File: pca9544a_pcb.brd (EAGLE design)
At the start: 43 x 43 mm, 37 parts, among them IC1 PCA9544ABS, X6 TSW-102-02-S-S-RA, X7 TSW-102-02-S-S-RA, X8 TSW-102-02-S-S-RA, X9 TSW-102-02-S-S-RA

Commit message: gerber out
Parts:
- GIT1: value b5c31e5 -> dcc5f2d
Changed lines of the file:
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@@
 </autorouter>
 <elements>
-<element name="GIT1" library="git-revision" package="GIT-REVISION_1.2" value="b5c31e5" x="32" y="37">
+<element name="GIT1" library="git-revision" package="GIT-REVISION_1.2" value="dcc5f2d" x="32" y="37">
 <attribute name="NOT_COMPONENT" value="YES" x="32" y="37" size="1.778" layer="27" display="off"/>
 </element>

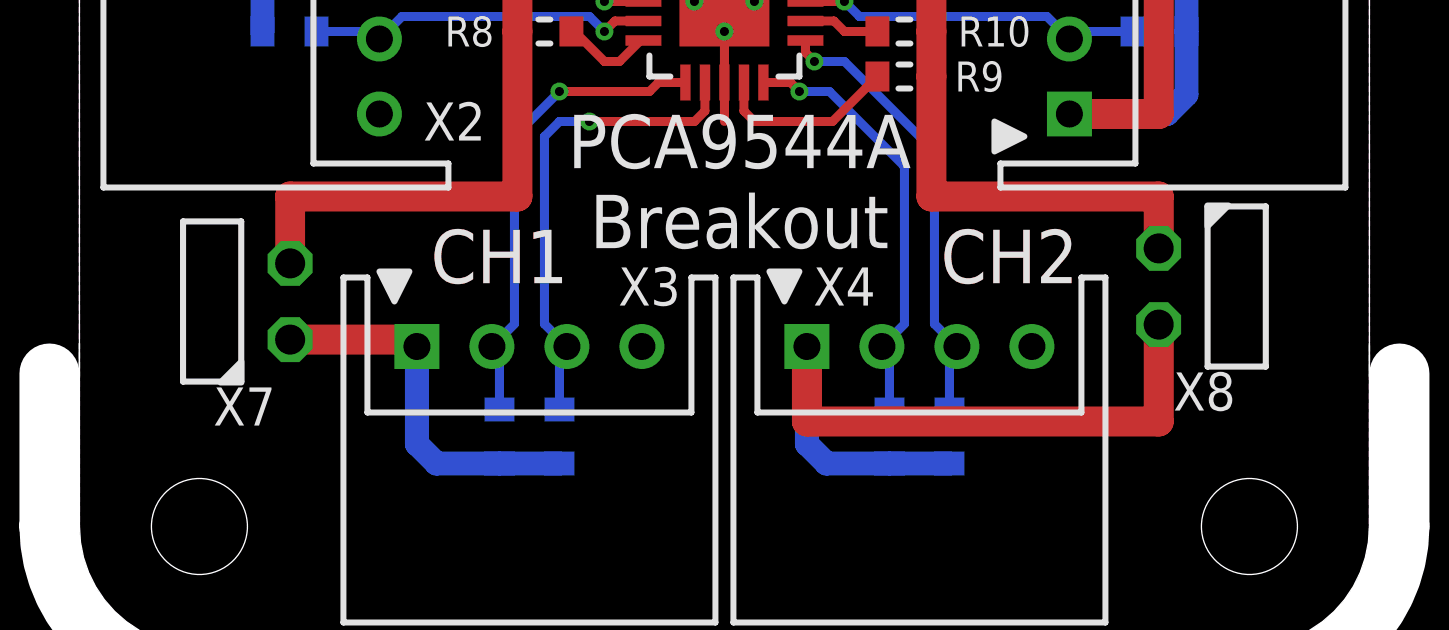
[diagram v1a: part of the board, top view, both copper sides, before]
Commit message: moved X7 and X8 headers
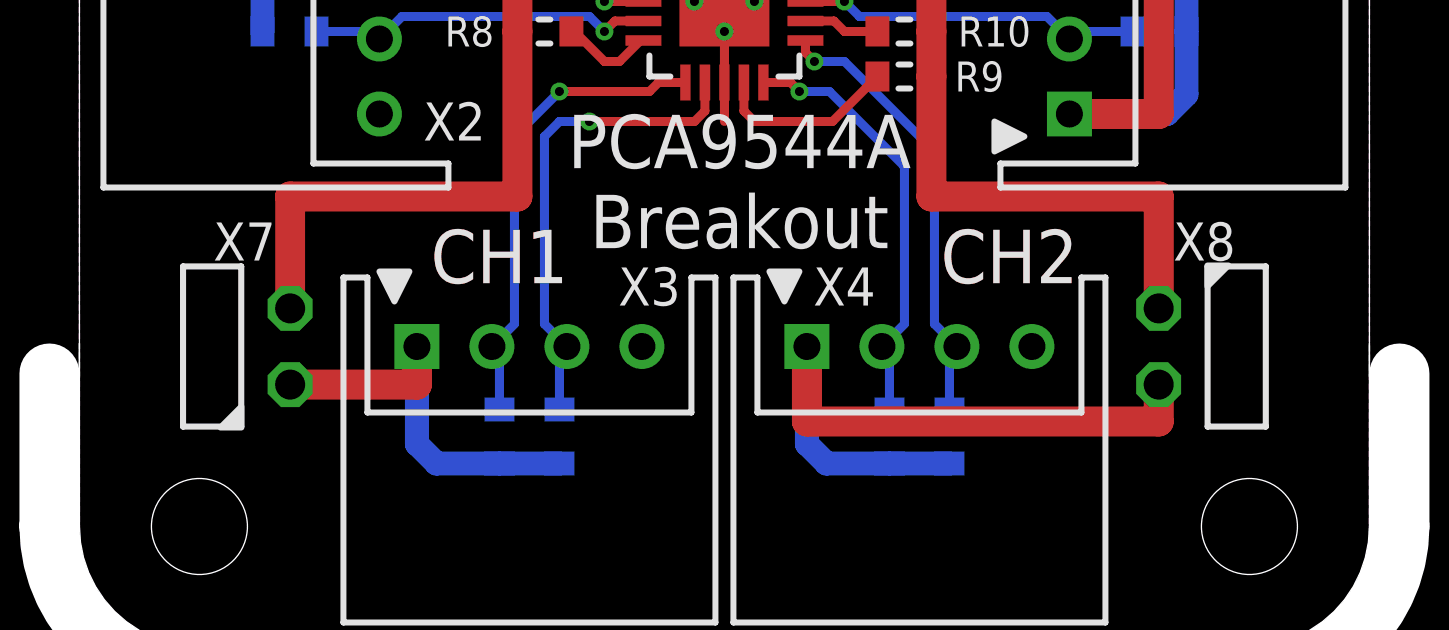
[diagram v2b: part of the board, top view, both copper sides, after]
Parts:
- moved X8 2.00 mm to (37.5, 10.0)
- moved X7 1.50 mm to (5.50, 10.0)
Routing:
- net VCC: track 96.7 -> 100.2 mm
- net N$21: track 25.7 -> 23.7 mm
- net N$20: track 12.7 -> 13.8 mm
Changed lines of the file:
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@@
 <attribute name="VALUE" x="-1.5" y="26.6" size="1" layer="27" ratio="20"/>
 </element>
-<element name="X7" library="con-samtec.local" package="TSW-102-02-S-S-RA" value="TSW-102-02-S-S-RA" x="5.5" y="11.5" smashed="yes" rot="R270">
-<attribute name="NAME" x="5.5" y="8" size="1.27" layer="25" ratio="16" align="center"/>
-<attribute name="VALUE" x="-1.5" y="7.1" size="1" layer="27" ratio="20"/>
+<element name="X7" library="con-samtec.local" package="TSW-102-02-S-S-RA" value="TSW-102-02-S-S-RA" x="5.5" y="10" smashed="yes" rot="R270">
+<attribute name="NAME" x="5.5" y="13.5" size="1.27" layer="25" ratio="16" align="center"/>
+<attribute name="VALUE" x="-1.5" y="5.6" size="1" layer="27" ratio="20"/>
 </element>
-<element name="X8" library="con-samtec.local" package="TSW-102-02-S-S-RA" value="TSW-102-02-S-S-RA" x="37.5" y="12" smashed="yes" rot="R90">
-<attribute name="NAME" x="37.5" y="8.5" size="1.27" layer="25" ratio="16" rot="R180" align="center"/>
-<attribute name="VALUE" x="44.5" y="16.4" size="1" layer="27" ratio="20" rot="R180"/>
+<element name="X8" library="con-samtec.local" package="TSW-102-02-S-S-RA" value="TSW-102-02-S-S-RA" x="37.5" y="10" smashed="yes" rot="R90">
+<attribute name="NAME" x="37.5" y="13.5" size="1.27" layer="25" ratio="16" rot="R180" align="center"/>
+<attribute name="VALUE" x="44.5" y="14.4" size="1" layer="27" ratio="20" rot="R180"/>
 </element>
 <element name="X9" library="con-samtec.local" package="TSW-102-02-S-S-RA" value="TSW-102-02-S-S-RA" x="37.5" y="31" smashed="yes" rot="R90">
@@
 <wire x1="14.6" y1="20.5" x2="14.6" y2="15" width="1" layer="1"/>
 <wire x1="14.6" y1="15" x2="7.024" y2="15" width="1" layer="1"/>
-<wire x1="7.024" y1="15" x2="7.024" y2="12.77" width="1" layer="1"/>
+<wire x1="7.024" y1="15" x2="7.024" y2="11.27" width="1" layer="1"/>
 <wire x1="28.4" y1="19" x2="28.4" y2="15" width="1" layer="1"/>
 <wire x1="28.4" y1="15" x2="35.976" y2="15" width="1" layer="1"/>
-<wire x1="35.976" y1="15" x2="35.976" y2="13.27" width="1" layer="1"/>
+<wire x1="35.976" y1="15" x2="35.976" y2="11.27" width="1" layer="1"/>
 </signal>
 <signal name="N$19">
@@
 <wire x1="14" y1="6.1" x2="16" y2="6.1" width="0.8" layer="16"/>
 <contactref element="X7" pad="1"/>
-<wire x1="7.024" y1="10.23" x2="11.25" y2="10.23" width="1" layer="1"/>
-<wire x1="11.25" y1="10.23" x2="11.25" y2="10" width="1" layer="1"/>
+<wire x1="7.024" y1="8.73" x2="11.25" y2="8.73" width="1" layer="1"/>
+<wire x1="11.25" y1="8.73" x2="11.25" y2="10" width="1" layer="1"/>
 </signal>
 <signal name="N$21">
@@
 <wire x1="24.25" y1="10" x2="24.25" y2="6.75" width="0.8" layer="16"/>
 <contactref element="X8" pad="2"/>
-<wire x1="35.976" y1="10.73" x2="35.976" y2="7.5" width="1" layer="1"/>
+<wire x1="35.976" y1="8.73" x2="35.976" y2="7.5" width="1" layer="1"/>
 <wire x1="35.976" y1="7.5" x2="24.25" y2="7.5" width="1" layer="1"/>
 <wire x1="24.25" y1="7.5" x2="24.25" y2="10" width="1" layer="1"/>

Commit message: gerber out
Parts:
- GIT1: value dcc5f2d -> 4eef362
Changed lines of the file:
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@@
 </autorouter>
 <elements>
-<element name="GIT1" library="git-revision" package="GIT-REVISION_1.2" value="dcc5f2d" x="32" y="37">
+<element name="GIT1" library="git-revision" package="GIT-REVISION_1.2" value="4eef362" x="32" y="37">
 <attribute name="NOT_COMPONENT" value="YES" x="32" y="37" size="1.778" layer="27" display="off"/>
 </element>
